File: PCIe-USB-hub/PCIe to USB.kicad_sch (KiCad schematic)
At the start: 1 part

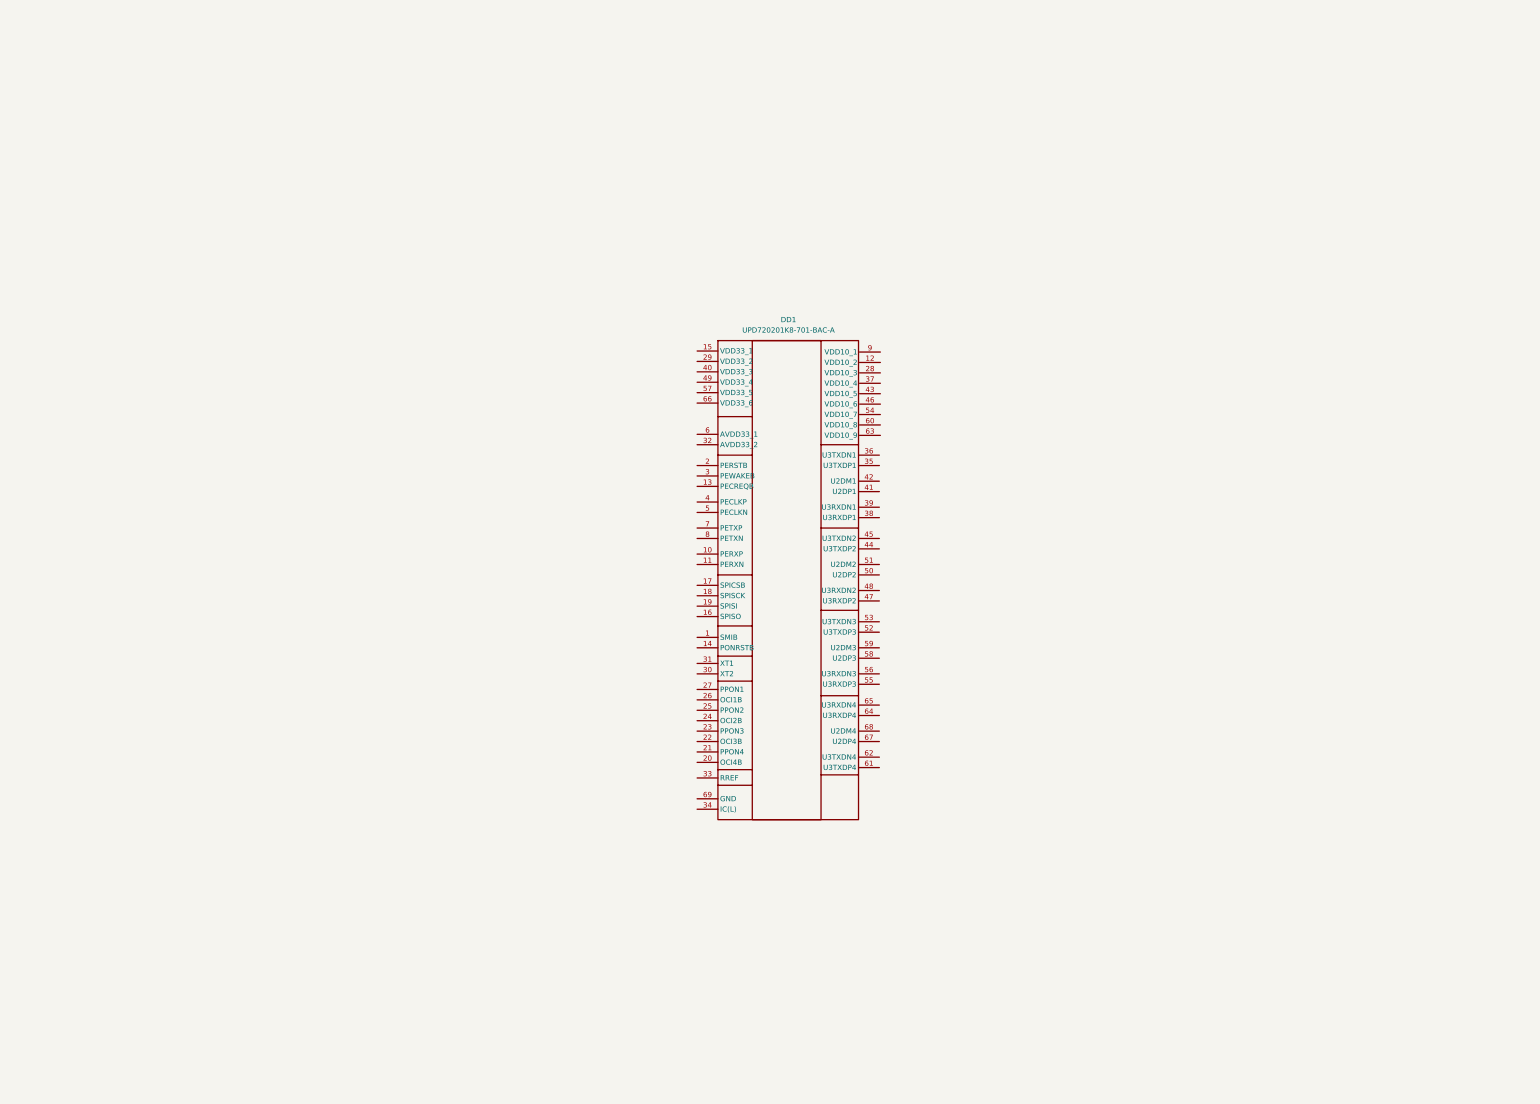
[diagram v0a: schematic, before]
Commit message: Изменение иерархии схемы + на схеме теперь все линии USB соединены
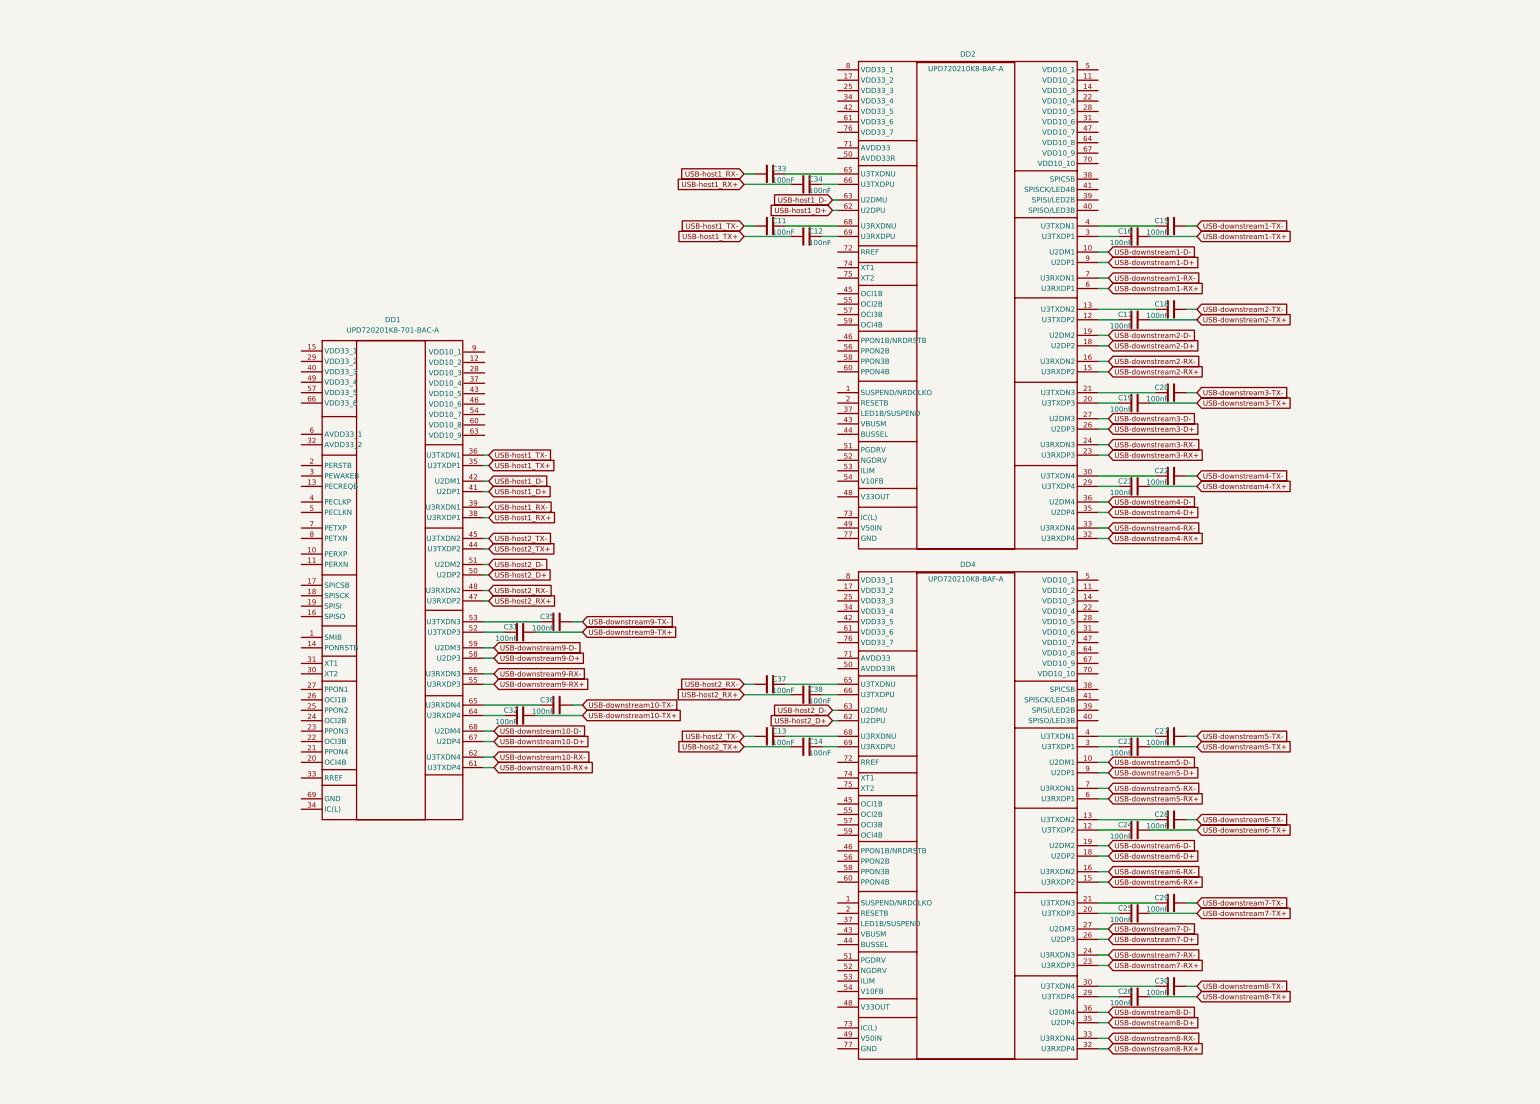
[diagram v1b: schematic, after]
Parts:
- added C11, C12, C13, C14, C15, C16, C17, C18, C19, C20, C21, C22, C23, C24, C25, C26, C27, C28, C29, C30, C31, C32, C33, C34, C35, C36, C37, C38: 100nF, Capacitor_SMD:C_0402_1005Metric, symbol Device:C
- added DD2, DD4: UPD720210K8-BAF-A, Package_DFN_QFN:QFN-76-1EP_9x9mm_P0.4mm_EP5.81x6.31mm, symbol UPD720210K8-BAF-A:UPD720210K8-BAF-A
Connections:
- net USB-host1_TX+: now reaches DD1.35 (U3TXDP1)
- net USB-host1_TX+: now also C12.1
- net USB-host1_TX-: now reaches DD1.36 (U3TXDN1)
- net USB-host1_TX-: now also C11.1
- net USB-host1_RX+: now reaches DD1.38 (U3RXDP1)
- net USB-host1_RX+: now also C34.1
- net USB-host1_RX-: now reaches DD1.39 (U3RXDN1)
- net USB-host1_RX-: now also C33.1
- net USB-host1_D+: now reaches DD1.41 (U2DP1)
- net USB-host1_D+: now also DD2.62 (U2DPU)
- net USB-host1_D-: now reaches DD1.42 (U2DM1)
- net USB-host1_D-: now also DD2.63 (U2DMU)
- net USB-host2_TX+: now reaches DD1.44 (U3TXDP2)
- net USB-host2_TX+: now also C14.1
- net USB-host2_TX-: now reaches DD1.45 (U3TXDN2)
- net USB-host2_TX-: now also C13.1
- net USB-host2_RX+: now reaches DD1.47 (U3RXDP2)
- net USB-host2_RX+: now also C38.1
- net USB-host2_RX-: now reaches DD1.48 (U3RXDN2)
- net USB-host2_RX-: now also C37.1
- net USB-host2_D+: now reaches DD1.50 (U2DP2)
- net USB-host2_D+: now also DD4.62 (U2DPU)
- net USB-host2_D-: now reaches DD1.51 (U2DM2)
- net USB-host2_D-: now also DD4.63 (U2DMU)
- net at DD1.52 (U3TXDP3): now also C31.2
- net at DD1.53 (U3TXDN3): now also C35.2
- net USB-downstream9-RX+: now reaches DD1.55 (U3RXDP3)
- net USB-downstream9-RX-: now reaches DD1.56 (U3RXDN3)
- net USB-downstream9-D+: now reaches DD1.58 (U2DP3)
- net USB-downstream9-D-: now reaches DD1.59 (U2DM3)
- net USB-downstream10-RX+: now reaches DD1.61 (U3TXDP4)
- net USB-downstream10-RX-: now reaches DD1.62 (U3TXDN4)
- net at DD1.64 (U3RXDP4): now also C32.2
- net at DD1.65 (U3RXDN4): now also C36.2
- net USB-downstream10-D+: now reaches DD1.67 (U2DP4)
- net USB-downstream10-D-: now reaches DD1.68 (U2DM4)
- new net: C13.2, DD4.68 (U3RXDNU)
- new net: C16.2, DD2.3 (U3TXDP1)
- new net: C28.2, DD4.13 (U3TXDN2)
- new net: C27.2, DD4.4 (U3TXDN1)
- new net: C23.2, DD4.3 (U3TXDP1)
- new net: C15.2, DD2.4 (U3TXDN1)
- new net: C29.2, DD4.21 (U3TXDN3)
- new net: C37.2, DD4.65 (U3TXDNU)
- new net: C17.2, DD2.12 (U3TXDP2)
- new net: C18.2, DD2.13 (U3TXDN2)
- new net: C19.2, DD2.20 (U3TXDP3)
- new net: C20.2, DD2.21 (U3TXDN3)
- new net: C21.2, DD2.29 (U3TXDP4)
- new net: C22.2, DD2.30 (U3TXDN4)
- new net: C33.2, DD2.65 (U3TXDNU)
- new net: C34.2, DD2.66 (U3TXDPU)
- new net: C11.2, DD2.68 (U3RXDNU)
- new net: C12.2, DD2.69 (U3RXDPU)
- new net: C30.2, DD4.30 (U3TXDN4)
- new net: C24.2, DD4.12 (U3TXDP2)
- new net: C14.2, DD4.69 (U3RXDPU)
- new net: C25.2, DD4.20 (U3TXDP3)
- new net: C38.2, DD4.66 (U3TXDPU)
- new net: C26.2, DD4.29 (U3TXDP4)
- new net USB-downstream1-D+: DD2.9 (U2DP1)
- new net USB-downstream1-D-: DD2.10 (U2DM1)
- new net USB-downstream1-RX+: DD2.6 (U3RXDP1)
- new net USB-downstream1-RX-: DD2.7 (U3RXDN1)
- new net USB-downstream1-TX+: C16.1
- new net USB-downstream1-TX-: C15.1
- new net USB-downstream10-TX+: C32.1
- new net USB-downstream10-TX-: C36.1
- new net USB-downstream2-D+: DD2.18 (U2DP2)
- new net USB-downstream2-D-: DD2.19 (U2DM2)
- new net USB-downstream2-RX+: DD2.15 (U3RXDP2)
- new net USB-downstream2-RX-: DD2.16 (U3RXDN2)
- new net USB-downstream2-TX+: C17.1
- new net USB-downstream2-TX-: C18.1
- new net USB-downstream3-D+: DD2.26 (U2DP3)
- new net USB-downstream3-D-: DD2.27 (U2DM3)
- new net USB-downstream3-RX+: DD2.23 (U3RXDP3)
- new net USB-downstream3-RX-: DD2.24 (U3RXDN3)
- new net USB-downstream3-TX+: C19.1
- new net USB-downstream3-TX-: C20.1
- new net USB-downstream4-D+: DD2.35 (U2DP4)
- new net USB-downstream4-D-: DD2.36 (U2DM4)
- new net USB-downstream4-RX+: DD2.32 (U3RXDP4)
- new net USB-downstream4-RX-: DD2.33 (U3RXDN4)
- new net USB-downstream4-TX+: C21.1
- new net USB-downstream4-TX-: C22.1
- new net USB-downstream5-D+: DD4.9 (U2DP1)
- new net USB-downstream5-D-: DD4.10 (U2DM1)
- new net USB-downstream5-RX+: DD4.6 (U3RXDP1)
- new net USB-downstream5-RX-: DD4.7 (U3RXDN1)
- new net USB-downstream5-TX+: C23.1
- new net USB-downstream5-TX-: C27.1
- new net USB-downstream6-D+: DD4.18 (U2DP2)
- new net USB-downstream6-D-: DD4.19 (U2DM2)
- new net USB-downstream6-RX+: DD4.15 (U3RXDP2)
- new net USB-downstream6-RX-: DD4.16 (U3RXDN2)
- new net USB-downstream6-TX+: C24.1
- new net USB-downstream6-TX-: C28.1
- new net USB-downstream7-D+: DD4.26 (U2DP3)
- new net USB-downstream7-D-: DD4.27 (U2DM3)
- new net USB-downstream7-RX+: DD4.23 (U3RXDP3)
- new net USB-downstream7-RX-: DD4.24 (U3RXDN3)
- new net USB-downstream7-TX+: C25.1
- new net USB-downstream7-TX-: C29.1
- new net USB-downstream8-D+: DD4.35 (U2DP4)
- new net USB-downstream8-D-: DD4.36 (U2DM4)
- new net USB-downstream8-RX+: DD4.32 (U3RXDP4)
- new net USB-downstream8-RX-: DD4.33 (U3RXDN4)
- new net USB-downstream8-TX+: C26.1
- new net USB-downstream8-TX-: C30.1
- new net USB-downstream9-TX+: C31.1
- new net USB-downstream9-TX-: C35.1
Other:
- moved on the sheet: DD1

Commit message: Доработка схемы, частичная конфигурация чипов
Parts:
- added C43, C44, C47, C48, C53, C54: 100nF, Capacitor_SMD:C_0402_1005Metric, symbol Device:C
- added C45, C46, C49, C50, C51, C52: 10pF, Capacitor_SMD:C_0402_1005Metric, symbol Device:C
- added D1, D2, D3: BAT54CW, Package_TO_SOT_SMD:SOT-323_SC-70, symbol Diode:BAT54CW
- added DD, DD5, DD6: MX25L8006EM2I-12G, Package_SO:SOP-8_3.9x4.9mm_P1.27mm, symbol Memory_Flash:MX25L3233FM1
- added R1, R10, R11, R18, R19, R20, R21, R22, R23, R24, R25, R26, R27, R28, R29, R3, R30, R31, R32, R33, R34, R35, R36, R37, R38, R39, R40, R41, R6, R7: 10K, PCM_Resistor_SMD_AKL:R_0603_1608Metric, symbol Device:R
- added R12, R13, R8, R9: 4.7K, PCM_Resistor_SMD_AKL:R_0603_1608Metric, symbol Device:R
- added R14, R17, R4: 680, PCM_Resistor_SMD_AKL:R_0603_1608Metric, symbol Device:R
- added R15, R16, R5: 1.6K, PCM_Resistor_SMD_AKL:R_0603_1608Metric, symbol Device:R
- added R2: 47K, PCM_Resistor_SMD_AKL:R_0603_1608Metric, symbol Device:R
- added TP1, TP10, TP11, TP12, TP2, TP3, TP4, TP5, TP6, TP7, TP8, TP9: TestPoint, TestPoint:TestPoint_Pad_D1.0mm, symbol Connector:TestPoint
- added Y1, Y2, Y3: X322524MQB4SI, Crystal:Crystal_SMD_Abracon_ABM8AIG-4Pin_3.2x2.5mm, symbol Device:Crystal_GND24
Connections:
- net PCIe-RX+: now reaches DD1.10 (PERXP)
- net PCIe-RX-: now reaches DD1.11 (PERXN)
- net at DD1.14 (PONRSTB): now also C44.1, D1.1, R3.2
- net SPISO: now reaches DD1.16 (SPISO)
- net SPISO: now also DD.2 (SO/SIO1), R2.2
- net SPISCK: now reaches DD1.17 (SPICSB)
- net SPISCK: now also DD.6 (SCLK)
- net SPICSB: now reaches DD1.18 (SPISCK)
- net SPICSB: now also DD.1 (~{CS})
- net SPISI: now reaches DD1.19 (SPISI)
- net SPISI: now also DD.5 (SI/SIO0)
- net PERST_PCIe: now reaches DD1.2 (PERSTB)
- net OCI10B: now reaches DD1.20 (OCI4B)
- net OCI10B: now also R23.1
- net PPON10: now reaches DD1.21 (PPON4)
- net OCI9B: now reaches DD1.22 (OCI3B)
- net OCI9B: now also R22.1
- net PPON9: now reaches DD1.23 (PPON3)
- net at DD1.24 (OCI2B): now also R19.1
- net at DD1.25 (PPON2): now also R20.1
- net at DD1.26 (OCI1B): now also R18.1
- net at DD1.27 (PPON1): now also R21.1
- net WAKE_PCIe: now reaches DD1.3 (PEWAKEB)
- net at DD1.30 (XT2): now also R4.1
- net at DD1.31 (XT1): now also C45.1, Y1.1
- net at DD1.33 (RREF): now also R5.1
- net Earth: now reaches DD1.34 (IC(L))
- net Earth: now also DD1.69 (GND), DD2.73 (IC(L)), DD2.77 (GND), DD4.73 (IC(L)), DD4.77 (GND), C43.2, C44.2, C45.2, C46.2, C47.2, C48.2, C49.2, C50.2, C51.2, C52.2, C53.2, C54.2, DD.4 (GND), DD5.4 (GND), DD6.4 (GND), R12.1, R13.1, R15.2, R16.2, R5.2, R8.1, R9.1, Y1.2, Y1.4, Y2.2, Y2.4, Y3.2, Y3.4
- net PCIe-CLK+: now reaches DD1.4 (PECLKP)
- net PCIe-CLK-: now reaches DD1.5 (PECLKN)
- net PCIe-TX+: now reaches DD1.7 (PETXP)
- net PCIe-TX-: now reaches DD1.8 (PETXN)
- net at DD2.2 (RESETB): now also C54.1, D3.1, R25.2
- net U1_LED1B: now reaches DD2.37 (LED1B/SUSPEND)
- net SPICSB1: now reaches DD2.38 (SPICSB)
- net SPICSB1: now also DD5.1 (~{CS})
- net SPISI1: now reaches DD2.39 (SPISI/LED2B)
- net SPISI1: now also DD5.5 (SI/SIO0), R6.2
- net SPISO1: now reaches DD2.40 (SPISO/LED3B)
- net SPISO1: now also DD5.2 (SO/SIO1), R9.2
- net SPISCK1: now reaches DD2.41 (SPISCK/LED4B)
- net SPISCK1: now also DD5.6 (SCLK), R8.2
- net OCI1B: now reaches DD2.45 (OCI1B)
- net OCI1B: now also R26.2
- net PPON1: now reaches DD2.46 (PPON1B/NRDRSTB)
- net PPON1: now also R30.2
- net at DD2.48 (V33OUT): now also TP5.1
- net at DD2.49 (V50IN): now also TP6.1
- net at DD2.51 (PGDRV): now also TP1.1
- net at DD2.52 (NGDRV): now also TP2.1
- net at DD2.53 (ILIM): now also TP3.1
- net at DD2.54 (V10FB): now also TP4.1
- net OCI2B: now reaches DD2.55 (OCI2B)
- net OCI2B: now also R27.2
- net PPON2: now reaches DD2.56 (PPON2B)
- net PPON2: now also R31.2
- net OCI3B: now reaches DD2.57 (OCI3B)
- net OCI3B: now also R28.2
- net PPON3: now reaches DD2.58 (PPON3B)
- net PPON3: now also R32.2
- net OCI4B: now reaches DD2.59 (OCI4B)
- net OCI4B: now also R29.2
- net PPON4: now reaches DD2.60 (PPON4B)
- net PPON4: now also R33.2
- net at DD2.72 (RREF): now also R16.1
- net at DD2.74 (XT1): now also C51.1, Y3.1
- net at DD2.75 (XT2): now also R17.1
- net at DD4.2 (RESETB): now also C53.1, D2.1, R24.2
- net U2_LED1B: now reaches DD4.37 (LED1B/SUSPEND)
- net SPICSB2: now reaches DD4.38 (SPICSB)
- net SPICSB2: now also DD6.1 (~{CS})
- net SPISI2: now reaches DD4.39 (SPISI/LED2B)
- net SPISI2: now also DD6.5 (SI/SIO0), R10.2
- net SPISO2: now reaches DD4.40 (SPISO/LED3B)
- net SPISO2: now also DD6.2 (SO/SIO1), R13.2
- net SPISCK2: now reaches DD4.41 (SPISCK/LED4B)
- net SPISCK2: now also DD6.6 (SCLK), R12.2
- net OCI5B: now reaches DD4.45 (OCI1B)
- net OCI5B: now also R34.2
- net PPON5: now reaches DD4.46 (PPON1B/NRDRSTB)
- net PPON5: now also R38.2
- net at DD4.48 (V33OUT): now also TP11.1
- net at DD4.49 (V50IN): now also TP12.1
- net at DD4.51 (PGDRV): now also TP7.1
- net at DD4.52 (NGDRV): now also TP8.1
- net at DD4.53 (ILIM): now also TP9.1
- net at DD4.54 (V10FB): now also TP10.1
- net OCI6B: now reaches DD4.55 (OCI2B)
- net OCI6B: now also R35.2
- net PPON6: now reaches DD4.56 (PPON2B)
- net PPON6: now also R39.2
- net OCI7B: now reaches DD4.57 (OCI3B)
- net OCI7B: now also R36.2
- net PPON7: now reaches DD4.58 (PPON3B)
- net PPON7: now also R40.2
- net OCI8B: now reaches DD4.59 (OCI4B)
- net OCI8B: now also R37.2
- net PPON8: now reaches DD4.60 (PPON4B)
- net PPON8: now also R41.2
- net at DD4.72 (RREF): now also R15.1
- net at DD4.74 (XT1): now also C49.1, Y2.1
- net at DD4.75 (XT2): now also R14.1
- new net: DD5.3 (~{WP}/SIO2), R7.2
- new net: C52.1, R17.2, Y3.3
- new net: DD.3 (~{WP}/SIO2), R1.2
- new net: C46.1, R4.2, Y1.3
- new net: C50.1, R14.2, Y2.3
- new net: DD6.3 (~{WP}/SIO2), R11.2
- new net +3.3V: DD.7 (~{HOLD}/SIO3), DD5.7 (~{HOLD}/SIO3), DD6.7 (~{HOLD}/SIO3)
- new net +3.3V_DUAL: C43.1, C47.1, C48.1, D1.3, D2.3, D3.3, DD.8 (VCC), DD5.8 (VCC), DD6.8 (VCC), R1.1, R10.1, R11.1, R18.2, R19.2, R2.1, R22.2, R23.2, R24.1, R25.1, R26.1, R27.1, R28.1, R29.1, R3.1, R30.1, R31.1, R32.1, R33.1, R34.1, R35.1, R36.1, R37.1, R38.1, R39.1, R40.1, R41.1, R6.1, R7.1
- no-connect marks 0 -> 11

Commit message: Чут чут модифицировал
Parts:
- renumbered DD to DD8
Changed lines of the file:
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@@
+	)
+	(symbol
+		(lib_id "power:+3.3V")
+		(at 210.82 147.32 0)
+		(unit 1)
+		(exclude_from_sim no)
+		(in_bom yes)
+		(on_board yes)
+		(dnp no)
+		(property "Reference" "#PWR073"
+			(at 210.82 151.13 0)
+			(effects
+				(font
+					(size 1.27 1.27)
+				)
+				(hide yes)
+			)
+		)
+		(property "Value" "+3.3V_DUAL"
+			(at 210.82 143.764 0)
+			(effects
+				(font
+					(size 1.27 1.27)
+				)
+			)
+		)
+		(property "Footprint" ""
+			(at 210.82 147.32 0)
+			(effects
+				(font
+					(size 1.27 1.27)
+				)
+				(hide yes)
+			)
+		)
+		(property "Datasheet" ""
+			(at 210.82 147.32 0)
+			(effects
+				(font
+					(size 1.27 1.27)
+				)
+				(hide yes)
+			)
+		)
+		(property "Description" "Power symbol creates a global label with name \"+3.3V\""
+			(at 210.82 147.32 0)
+			(effects
+				(font
+					(size 1.27 1.27)
+				)
+				(hide yes)
+			)
+		)
+		(pin "1"
+		)
+		(instances
+			(project "PCIe-USB-hub"
+				(path "/9ca96bdf-018d-455b-a724-78a2bbb0adec/09537bd2-8ad3-47b5-a113-3e1df9f3dc09"
+					(reference "#PWR073")
+					(unit 1)
+				)
+			)
+		)
 	)
 	(symbol
@@
 		(dnp no)
 		(fields_autoplaced yes)
-		(property "Reference" "DD"
+		(property "Reference" "DD8"
 			(at 58.42 120.904 0)
 			(effects
@@
 			(project ""
 				(path "/9ca96bdf-018d-455b-a724-78a2bbb0adec/09537bd2-8ad3-47b5-a113-3e1df9f3dc09"
-					(reference "DD")
-					(unit 1)
-				)
+					(reference "DD8")
+					(unit 1)
+				)
